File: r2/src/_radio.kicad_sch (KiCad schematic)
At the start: 49 parts, among them J8 DNP, U9 CC1200, Y2 40Mhz

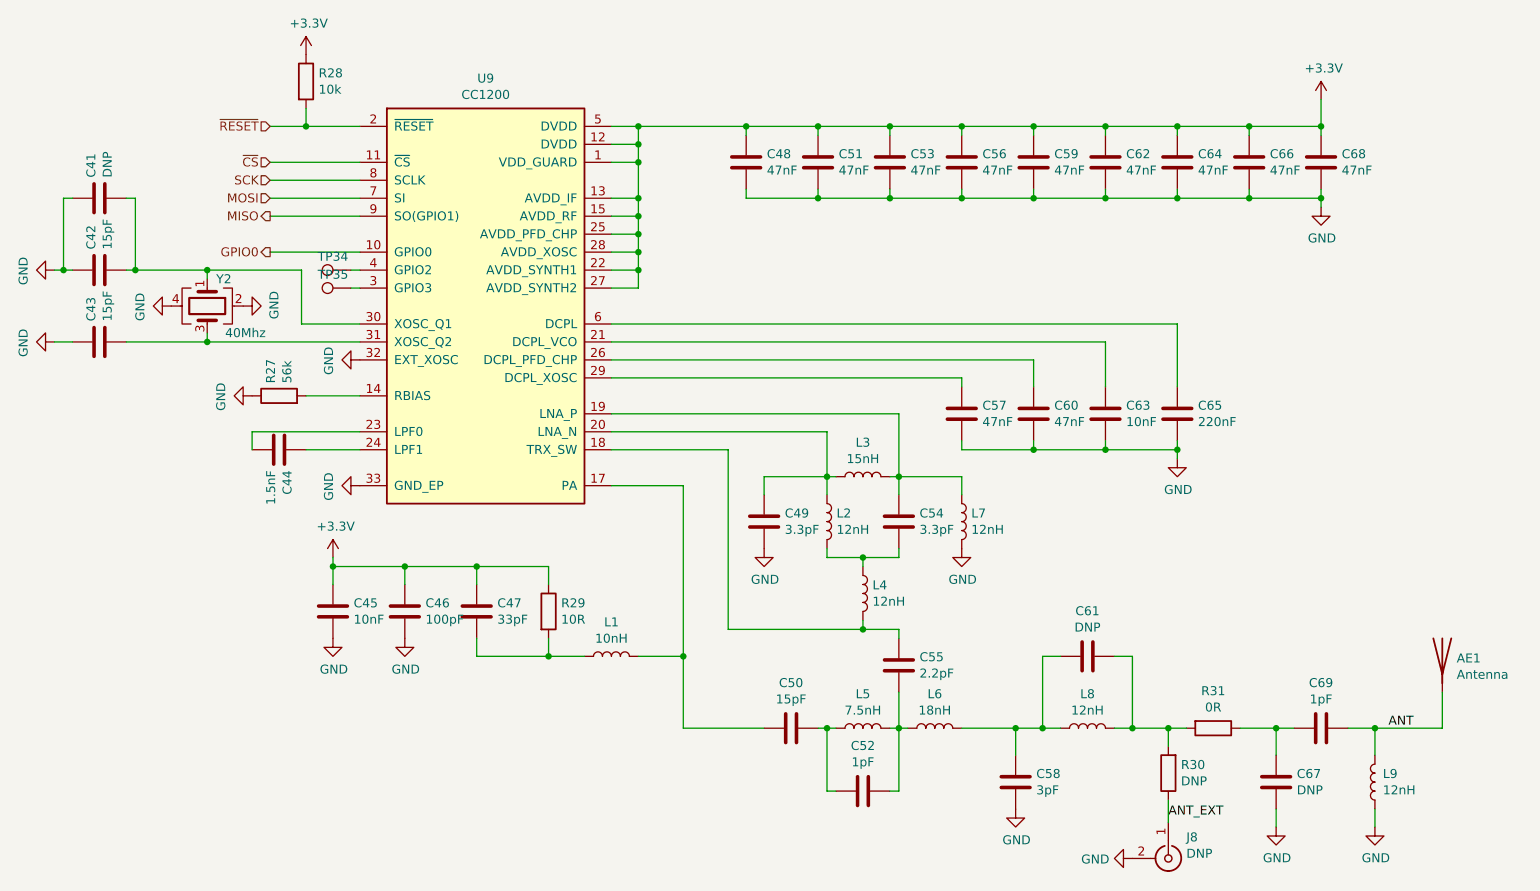
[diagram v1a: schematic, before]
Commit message: Fix off-grid ERC errors so whole schematic is on 1.27mm grid
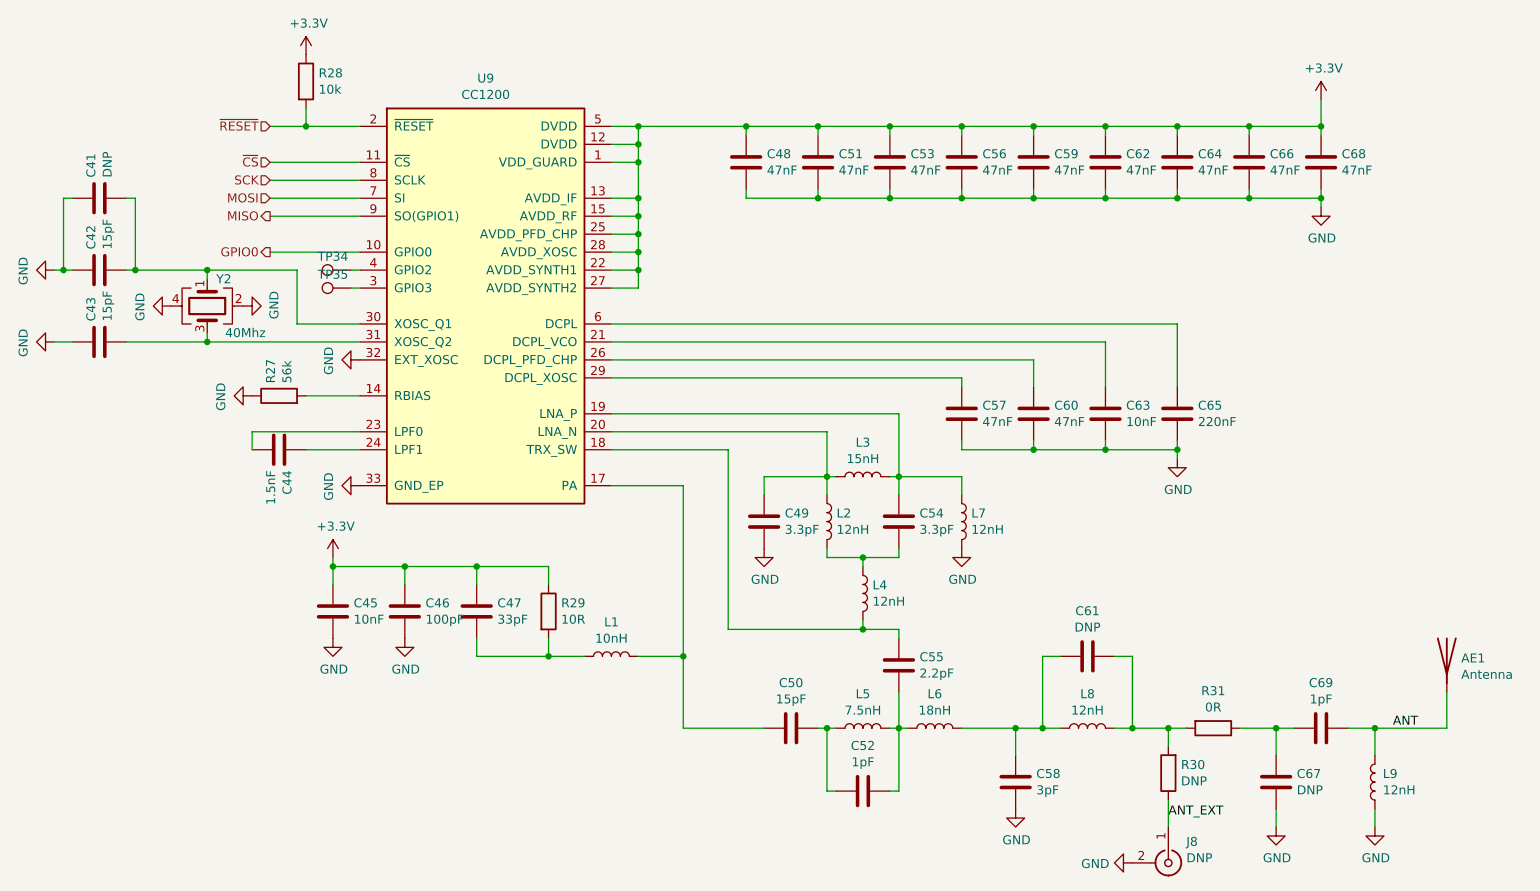
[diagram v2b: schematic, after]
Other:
- moved on the sheet: AE1, J8
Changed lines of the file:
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@@
     (stroke (width 0) (type default))
   )
-  (wire (pts (xy 189.23 146.685) (xy 189.23 143.51))
+  (wire (pts (xy 189.23 147.32) (xy 189.23 143.51))
     (stroke (width 0) (type default))
   )
@@
     (stroke (width 0) (type default))
   )
-  (wire (pts (xy 66.675 68.58) (xy 53.34 68.58))
+  (wire (pts (xy 66.04 68.58) (xy 53.34 68.58))
     (stroke (width 0) (type default))
   )
@@
     (stroke (width 0) (type default))
   )
-  (wire (pts (xy 227.965 133.35) (xy 227.965 128.27))
+  (wire (pts (xy 228.6 133.35) (xy 228.6 128.27))
     (stroke (width 0) (type default))
   )
@@
     (stroke (width 0) (type default))
   )
-  (wire (pts (xy 66.675 76.2) (xy 74.93 76.2))
+  (wire (pts (xy 66.04 76.2) (xy 74.93 76.2))
     (stroke (width 0) (type default))
   )
@@
     (stroke (width 0) (type default))
   )
-  (wire (pts (xy 218.44 133.35) (xy 227.965 133.35))
-    (stroke (width 0) (type default))
-  )
   (wire (pts (xy 146.05 118.11) (xy 146.05 119.38))
     (stroke (width 0) (type default))
@@
     (stroke (width 0) (type default))
   )
+  (wire (pts (xy 218.44 133.35) (xy 228.6 133.35))
+    (stroke (width 0) (type default))
+  )
   (wire (pts (xy 180.34 49.53) (xy 180.34 48.26))
     (stroke (width 0) (type default))
@@
     (stroke (width 0) (type default))
   )
-  (wire (pts (xy 66.675 76.2) (xy 66.675 68.58))
+  (wire (pts (xy 66.04 76.2) (xy 66.04 68.58))
     (stroke (width 0) (type default))
   )
@@
     (stroke (width 0) (type default))
   )
-  (label "ANT" (at 220.345 133.35 0) (fields_autoplaced)
+  (label "ANT" (at 220.98 133.35 0) (fields_autoplaced)
     (effects (font (size 1.27 1.27)) (justify left bottom))
   )
@@
     )
   )
-  (symbol (lib_id "Connector:Conn_Coaxial") (at 189.23 151.765 270) (unit 1)
-    (in_bom yes) (on_board yes) (dnp no)
-    (property "Reference" "J8" (at 191.77 148.7678 90)
-      (effects (font (size 1.27 1.27)) (justify left))
-    )
-    (property "Value" "DNP" (at 191.77 151.0792 90)
-      (effects (font (size 1.27 1.27)) (justify left))
-    )
-    (property "Footprint" "Connector_Coaxial:SMA_Amphenol_132134-10_Vertical" (at 189.23 151.765 0)
-      (effects (font (size 1.27 1.27)) hide)
-    )
-    (property "Datasheet" " ~" (at 189.23 151.765 0)
+  (symbol (lib_id "Connector:Conn_Coaxial") (at 189.23 152.4 270) (unit 1)
+    (in_bom yes) (on_board yes) (dnp no)
+    (property "Reference" "J8" (at 191.77 149.4028 90)
+      (effects (font (size 1.27 1.27)) (justify left))
+    )
+    (property "Value" "DNP" (at 191.77 151.7142 90)
+      (effects (font (size 1.27 1.27)) (justify left))
+    )
+    (property "Footprint" "Connector_Coaxial:SMA_Amphenol_132134-10_Vertical" (at 189.23 152.4 0)
+      (effects (font (size 1.27 1.27)) hide)
+    )
+    (property "Datasheet" " ~" (at 189.23 152.4 0)
       (effects (font (size 1.27 1.27)) hide)
     )
@@
     )
   )
-  (symbol (lib_id "power:GND") (at 184.15 151.765 270) (unit 1)
-    (in_bom yes) (on_board yes) (dnp no)
-    (property "Reference" "#PWR0146" (at 177.8 151.765 0)
-      (effects (font (size 1.27 1.27)) hide)
-    )
-    (property "Value" "GND" (at 180.8988 151.892 90)
+  (symbol (lib_id "power:GND") (at 184.15 152.4 270) (unit 1)
+    (in_bom yes) (on_board yes) (dnp no)
+    (property "Reference" "#PWR0146" (at 177.8 152.4 0)
+      (effects (font (size 1.27 1.27)) hide)
+    )
+    (property "Value" "GND" (at 180.8988 152.527 90)
       (effects (font (size 1.27 1.27)) (justify right))
     )
-    (property "Footprint" "" (at 184.15 151.765 0)
-      (effects (font (size 1.27 1.27)) hide)
-    )
-    (property "Datasheet" "" (at 184.15 151.765 0)
+    (property "Footprint" "" (at 184.15 152.4 0)
+      (effects (font (size 1.27 1.27)) hide)
+    )
+    (property "Datasheet" "" (at 184.15 152.4 0)
       (effects (font (size 1.27 1.27)) hide)
     )
@@
     )
   )
-  (symbol (lib_id "Device:Antenna") (at 227.965 123.19 0) (unit 1)
+  (symbol (lib_id "Device:Antenna") (at 228.6 123.19 0) (unit 1)
     (in_bom no) (on_board yes) (dnp no)
-    (property "Reference" "AE1" (at 229.997 123.4694 0)
-      (effects (font (size 1.27 1.27)) (justify left))
-    )
-    (property "Value" "Antenna" (at 229.997 125.7808 0)
-      (effects (font (size 1.27 1.27)) (justify left))
-    )
-    (property "Footprint" "jeffmakes-footprints:Antenna_TI_DN038" (at 227.965 123.19 0)
-      (effects (font (size 1.27 1.27)) hide)
-    )
-    (property "Datasheet" "~" (at 227.965 123.19 0)
-      (effects (font (size 1.27 1.27)) hide)
-    )
+    (property "Reference" "AE1" (at 230.632 123.4694 0)
+      (effects (font (size 1.27 1.27)) (justify left))
+    )
+    (property "Value" "Antenna" (at 230.632 125.7808 0)
+      (effects (font (size 1.27 1.27)) (justify left))
+    )
+    (property "Footprint" "jeffmakes-footprints:Antenna_TI_DN038" (at 228.6 123.19 0)
+      (effects (font (size 1.27 1.27)) hide)
+    )
+    (property "Datasheet" "~" (at 228.6 123.19 0)
+      (effects (font (size 1.27 1.27)) hide)
+    )

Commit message: Set title block contents
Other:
- company: (none) -> Monad Gottfried Ltd. 2023
- title: (none) -> Troopers 23 Badge
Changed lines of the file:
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@@
 (kicad_sch (version 20230409) (generator eeschema)
   (paper "A4")
+  (title_block
+    (title "Troopers 23 Badge")
+    (rev "r2")
+    (company "Monad Gottfried Ltd. 2023")
+    (comment 1 "for ERNW Enno Rey Netzwerke GmbH")
+  )
   (junction (at 140.97 133.35) (diameter 0) (color 0 0 0 0)
   )
